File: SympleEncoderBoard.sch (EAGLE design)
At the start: 31 parts, among them IC1 STM32F446RET6

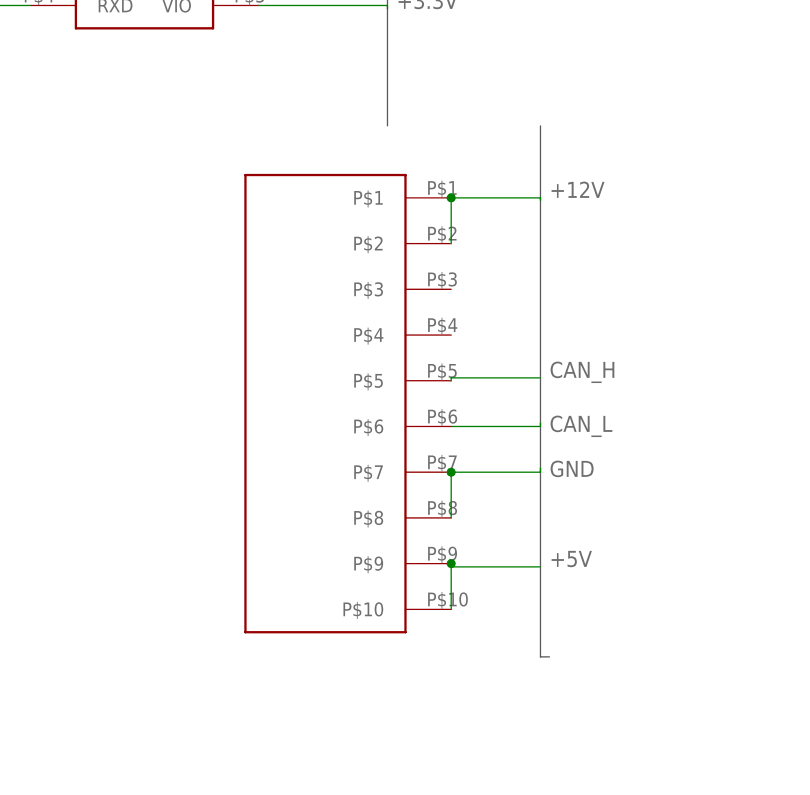
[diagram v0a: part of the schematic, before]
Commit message: コネクタのホール修正しました
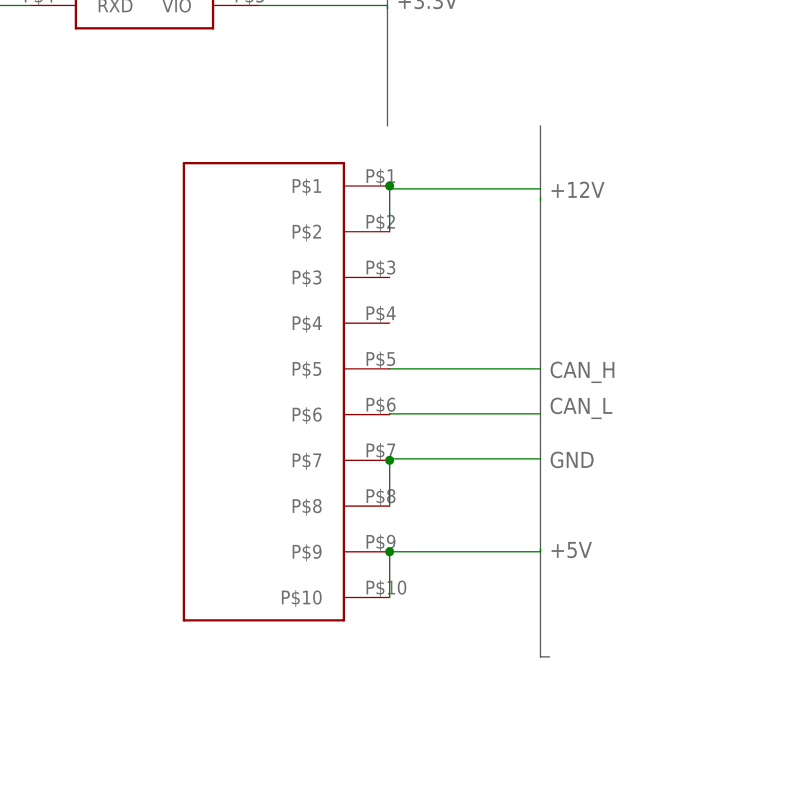
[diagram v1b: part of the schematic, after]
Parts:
- removed BOX10P-L1: BOX10PBOX10P-L, user_conector:BOX10PBOX10P-L
- added U$4: BOX10PBOX10P-L, user_conector:BOX10PBOX10P-L
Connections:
- net +12V: now also U$4.P$1, U$4.P$2; no longer BOX10P-L1.P$1, BOX10P-L1.P$2
- net +5V: now also U$4.P$10, U$4.P$9; no longer BOX10P-L1.P$10, BOX10P-L1.P$9
- net CAN_H: now also U$4.P$5; no longer BOX10P-L1.P$5
- net CAN_L: now also U$4.P$6; no longer BOX10P-L1.P$6
- net GND: now also U$4.P$7, U$4.P$8; no longer BOX10P-L1.P$7, BOX10P-L1.P$8
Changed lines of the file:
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@@
 <setting verticaltext="up"/>
 </settings>
-<grid distance="1" unitdist="mm" unit="mm" style="lines" multiple="1" display="yes" altdistance="0.1" altunitdist="mm" altunit="mm"/>
+<grid distance="1" unitdist="mm" unit="mm" style="lines" multiple="1" display="yes" altdistance="0.01" altunitdist="inch" altunit="mm"/>
 <layers>
 <layer number="1" name="Top" color="4" fill="1" visible="no" active="no"/>
@@
 <part name="ENCODER_X" library="S4B-XH-A_LF__SN_" deviceset="S4B-XH-A_LF__SN_" device=""/>
 <part name="ENCODER_Y" library="S4B-XH-A_LF__SN_" deviceset="S4B-XH-A_LF__SN_" device=""/>
-<part name="BOX10P-L1" library="user_conector" deviceset="BOX10P" device="BOX10P-L"/>
 <part name="U$2" library="SympleEncoderBoard" deviceset="BP5293-33" device=""/>
 <part name="R3" library="rcl" library_urn="urn:adsk.eagle:library:334" deviceset="R-US_" device="R0603" package3d_urn="urn:adsk.eagle:package:23555/3" value="150"/>
@@
 <part name="C7" library="rcl" library_urn="urn:adsk.eagle:library:334" deviceset="C-EU" device="C0603" package3d_urn="urn:adsk.eagle:package:23616/2" value="0.1μ"/>
 <part name="GYRO" library="B4B-XH-A_LF__SN_" deviceset="B4B-XH-A_LF__SN_" device=""/>
+<part name="U$4" library="user_conector" deviceset="BOX10P" device="BOX10P-L"/>
 </parts>
 <sheets>
@@
 <attribute name="VALUE" x="223.51" y="-5.92" size="1.778" layer="96" align="center-left"/>
 </instance>
-<instance part="BOX10P-L1" gate="G$1" x="-4" y="16" smashed="yes"/>
 <instance part="U$2" gate="G$1" x="41.18" y="133.46" smashed="yes"/>
 <instance part="R3" gate="G$1" x="32" y="93" smashed="yes" rot="R90">
@@
 <attribute name="VALUE" x="223.51" y="-45.92" size="1.778" layer="96" align="center-left"/>
 </instance>
+<instance part="U$4" gate="G$1" x="-21" y="-3" smashed="yes"/>
 </instances>
 <busses>
@@
 </segment>
 <segment>
-<pinref part="BOX10P-L1" gate="G$1" pin="P$7"/>
-<wire x1="11" y1="-14" x2="11" y2="-14.48" width="0.1524" layer="91"/>
-<wire x1="11" y1="-14.48" x2="1.08" y2="-14.48" width="0.1524" layer="91"/>
-<pinref part="BOX10P-L1" gate="G$1" pin="P$8"/>
-<wire x1="1.08" y1="-14.48" x2="1.08" y2="-19.56" width="0.1524" layer="91"/>
-<junction x="1.08" y="-14.48"/>
-<label x="12" y="-15" size="1.778" layer="95"/>
-</segment>
-<segment>
 <pinref part="U$3" gate="G$1" pin="VSS"/>
 <wire x1="-45.7" y1="47.54" x2="-45.7" y2="48" width="0.1524" layer="91"/>
@@
 <label x="130" y="-5" size="1.778" layer="95" rot="R90"/>
 </segment>
+<segment>
+<pinref part="U$4" gate="G$1" pin="P$7"/>
+<wire x1="11" y1="-13" x2="-5.76" y2="-13" width="0.1524" layer="91"/>
+<wire x1="-5.76" y1="-13" x2="-5.76" y2="-13.16" width="0.1524" layer="91"/>
+<pinref part="U$4" gate="G$1" pin="P$8"/>
+<wire x1="-5.76" y1="-18.24" x2="-5.76" y2="-13.16" width="0.1524" layer="91"/>
+<junction x="-5.76" y="-13.16"/>
+<label x="12" y="-14" size="1.778" layer="95"/>
+</segment>
 </net>
 <net name="NRST" class="0">
@@
 <segment>
 <wire x1="-60" y1="47.92" x2="-60" y2="48" width="0.1524" layer="91"/>
-</segment>
-<segment>
-<pinref part="BOX10P-L1" gate="G$1" pin="P$10"/>
-<pinref part="BOX10P-L1" gate="G$1" pin="P$9"/>
-<wire x1="1.08" y1="-29.72" x2="1.08" y2="-24.64" width="0.1524" layer="91"/>
-<wire x1="11" y1="-25" x2="1.08" y2="-25" width="0.1524" layer="91"/>
-<wire x1="1.08" y1="-25" x2="1.08" y2="-24.64" width="0.1524" layer="91"/>
-<junction x="1.08" y="-24.64"/>
-<label x="12" y="-25" size="1.778" layer="95"/>
 </segment>
 <segment>
@@
 <label x="195" y="-59" size="1.778" layer="95"/>
 </segment>
+<segment>
+<pinref part="U$4" gate="G$1" pin="P$10"/>
+<pinref part="U$4" gate="G$1" pin="P$9"/>
+<wire x1="-5.76" y1="-28.4" x2="-5.76" y2="-23.32" width="0.1524" layer="91"/>
+<wire x1="11" y1="-23" x2="11" y2="-23.32" width="0.1524" layer="91"/>
+<wire x1="11" y1="-23.32" x2="-5.76" y2="-23.32" width="0.1524" layer="91"/>
+<junction x="-5.76" y="-23.32"/>
+<label x="12" y="-24" size="1.778" layer="95"/>
+</segment>
 </net>
 <net name="CAN_L" class="0">
-<segment>
-<pinref part="BOX10P-L1" gate="G$1" pin="P$6"/>
-<wire x1="11" y1="-9" x2="11" y2="-9.4" width="0.1524" layer="91"/>
-<wire x1="11" y1="-9.4" x2="1.08" y2="-9.4" width="0.1524" layer="91"/>
-<label x="12" y="-10" size="1.778" layer="95"/>
-</segment>
 <segment>
 <pinref part="U$3" gate="G$1" pin="CANL"/>
@@
 <label x="-5" y="40" size="1.778" layer="95"/>
 </segment>
+<segment>
+<pinref part="U$4" gate="G$1" pin="P$6"/>
+<wire x1="11" y1="-8" x2="-5.76" y2="-8" width="0.1524" layer="91"/>
+<wire x1="-5.76" y1="-8" x2="-5.76" y2="-8.08" width="0.1524" layer="91"/>
+<label x="12" y="-8" size="1.778" layer="95"/>
+</segment>
 </net>
 <net name="CAN_H" class="0">
-<segment>
-<pinref part="BOX10P-L1" gate="G$1" pin="P$5"/>
-<wire x1="11" y1="-4" x2="1.08" y2="-4" width="0.1524" layer="91"/>
-<wire x1="1.08" y1="-4" x2="1.08" y2="-4.32" width="0.1524" layer="91"/>
-<label x="12" y="-4" size="1.778" layer="95"/>
-</segment>
 <segment>
 <pinref part="U$3" gate="G$1" pin="CANH"/>
@@
 <label x="-5" y="50" size="1.778" layer="95"/>
 </segment>
+<segment>
+<pinref part="U$4" gate="G$1" pin="P$5"/>
+<wire x1="11" y1="-3" x2="-5.76" y2="-3" width="0.1524" layer="91"/>
+<label x="12" y="-4" size="1.778" layer="95"/>
+</segment>
 </net>
 <net name="+12V" class="0">
@@
 </segment>
 <segment>
-<pinref part="BOX10P-L1" gate="G$1" pin="P$1"/>
-<pinref part="BOX10P-L1" gate="G$1" pin="P$2"/>
-<wire x1="1.08" y1="16" x2="1.08" y2="10.92" width="0.1524" layer="91"/>
-<wire x1="11" y1="16" x2="1.08" y2="16" width="0.1524" layer="91"/>
-<junction x="1.08" y="16"/>
+<pinref part="U$4" gate="G$1" pin="P$2"/>
+<pinref part="U$4" gate="G$1" pin="P$1"/>
+<wire x1="-5.76" y1="12.24" x2="-5.76" y2="17.32" width="0.1524" layer="91"/>
+<wire x1="11" y1="17" x2="-5.76" y2="17" width="0.1524" layer="91"/>
+<wire x1="-5.76" y1="17" x2="-5.76" y2="17.32" width="0.1524" layer="91"/>
+<junction x="-5.76" y="17.32"/>
 <label x="12" y="16" size="1.778" layer="95"/>
 </segment>

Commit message: 集合抵抗の値を変えました
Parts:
- R_I1: value 150 -> 1k
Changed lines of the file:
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@@
 <setting verticaltext="up"/>
 </settings>
-<grid distance="1" unitdist="mm" unit="mm" style="lines" multiple="1" display="yes" altdistance="0.01" altunitdist="inch" altunit="mm"/>
+<grid distance="0.1" unitdist="inch" unit="inch" style="lines" multiple="1" display="no" altdistance="0.01" altunitdist="inch" altunit="inch"/>
 <layers>
 <layer number="1" name="Top" color="4" fill="1" visible="no" active="no"/>
@@
 <part name="RX" library="led" library_urn="urn:adsk.eagle:library:259" deviceset="LED" device="CHIPLED_0603" package3d_urn="urn:adsk.eagle:package:15822/2"/>
 <part name="ACK" library="led" library_urn="urn:adsk.eagle:library:259" deviceset="LED" device="CHIPLED_0603" package3d_urn="urn:adsk.eagle:package:15822/2"/>
-<part name="R_I1" library="user_rcl" deviceset="R_SHUGOU" device="" value="150"/>
+<part name="R_I1" library="user_rcl" deviceset="R_SHUGOU" device="" value="1k"/>
 <part name="POWER" library="led" library_urn="urn:adsk.eagle:library:259" deviceset="LED" device="CHIPLED_0603" package3d_urn="urn:adsk.eagle:package:15822/2"/>
 <part name="OSC1" library="user_osc" deviceset="CSTN#" device=""/>

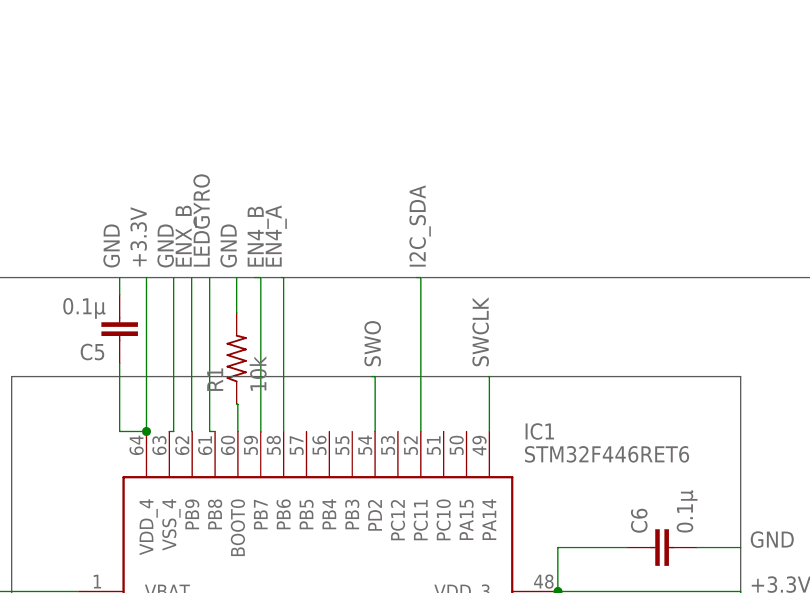
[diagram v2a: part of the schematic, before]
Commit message: SDAピンをPC11からPC12に修正した。
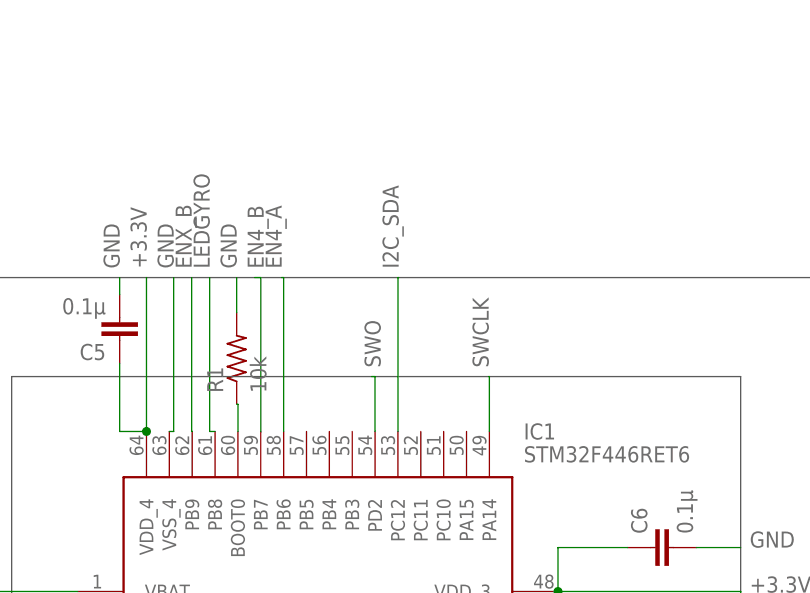
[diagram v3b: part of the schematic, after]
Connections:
- net I2C_SDA: now also IC1.PC12; no longer IC1.PC11
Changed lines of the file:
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@@
 <setting verticaltext="up"/>
 </settings>
-<grid distance="0.1" unitdist="inch" unit="inch" style="lines" multiple="1" display="no" altdistance="0.01" altunitdist="inch" altunit="inch"/>
+<grid distance="1" unitdist="mm" unit="mm" style="lines" multiple="1" display="yes" altdistance="0.01" altunitdist="inch" altunit="mm"/>
 <layers>
 <layer number="1" name="Top" color="4" fill="1" visible="no" active="no"/>
@@
 <net name="I2C_SDA" class="0">
 <segment>
-<pinref part="IC1" gate="G$1" pin="PC11"/>
-<wire x1="124.46" y1="88.9" x2="124.46" y2="106" width="0.1524" layer="91"/>
-<wire x1="124.46" y1="106" x2="124" y2="106" width="0.1524" layer="91"/>
-<label x="125" y="107" size="1.778" layer="95" rot="R90"/>
-</segment>
-<segment>
 <pinref part="GYRO" gate="G$1" pin="3"/>
 <wire x1="207" y1="-56.08" x2="200" y2="-56.08" width="0.1524" layer="91"/>
@@
 <label x="189" y="-56" size="1.778" layer="95"/>
 </segment>
-</net>
+<segment>
+<pinref part="IC1" gate="G$1" pin="PC12"/>
+<wire x1="121.92" y1="88.9" x2="121.92" y2="106" width="0.1524" layer="91"/>
+<wire x1="121.92" y1="106" x2="122" y2="106" width="0.1524" layer="91"/>
+<label x="122" y="107" size="1.778" layer="95" rot="R90"/>
+</segment>
+</net>
